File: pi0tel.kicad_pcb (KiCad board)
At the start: 2 copper layers, 10 parts, among them J1 DIN-5_180degree, J2 RPi_GPIO, Q1 BSS138, U1 LM2596S-5

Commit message: grrr
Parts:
- removed 10k1: R, Resistor_SMD:R_0805_2012Metric_Pad1.15x1.40mm_HandSolder
- added ?: , RPi_Hat:RPi_Hat_Mounting_Hole, F.Cu at (16.0, 51.0)
- added ?: , RPi_Hat:RPi_Hat_Mounting_Hole, F.Cu at (74.0, 28.0)
- added ?: , RPi_Hat:RPi_Hat_Mounting_Hole, F.Cu at (74.0, 51.0)
- added ?: , RPi_Hat:RPi_Hat_Mounting_Hole, F.Cu at (16.0, 28.0)
- added R2: 10k, Resistor_SMD:R_0805_2012Metric_Pad1.15x1.40mm_HandSolder, F.Cu at (48.3, 34.3)
- moved Q1 100.5 mm to (54.6, 34.3), turned to 180 degrees
- moved R1 100.5 mm to (62.2, 34.3), turned to 180 degrees
- moved U1 95.2 mm to (27.9, 41.9), turned to 90 degrees
- moved C1 90.6 mm to (17.8, 36.8), turned to 90 degrees
- moved C2 75.4 mm to (20.3, 36.8), turned to 90 degrees
- moved D1 74.4 mm to (15.2, 36.8), turned to 90 degrees
- moved L1 57.3 mm to (41.9, 47.0), turned to 270 degrees
- moved J2 47.7 mm to (20.9, 29.3), turned to 90 degrees
- moved J1 22.8 mm to (59.7, 47.0), turned to 180 degrees
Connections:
- C1 pad 1: GND -> /MinitelVcc
- J1 pad 5: GND -> /MinitelVcc
- U1 pad 1: GND -> /MinitelVcc
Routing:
- net /MinitelRx: track 0.00 -> 46.9 mm
- net +5V: track 0.00 -> 40.7 mm
- net Net-(D1-Pad1): track 0.00 -> 36.3 mm
- net /PiRx: track 0.00 -> 34.6 mm
- net /MinitelTx: track 0.00 -> 12.7 mm
- net /MinitelVcc: track 0.00 -> 12.6 mm
- added copper zone on F.Cu, net +3V3
- added copper zone on B.Cu, net GND
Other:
- board outline added: 65 x 30 mm
- net class Default: via_dia 0.8 -> 0.6
- rule pad_to_mask_clearance: 0.051 -> 0
- rule trace_min: 0.2 -> 0.01

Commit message: hmmm
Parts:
- J1: footprint footprints:din_5_econet_pcb_mount -> myelin-kicad:din_5_econet_pcb_mount
- moved C2 40.8 mm to (61.0, 40.6)
- moved D1 40.7 mm to (55.9, 34.3)
- moved R1 33.0 mm to (29.2, 33.0), turned to 90 degrees
- moved Q1 31.4 mm to (23.2, 34.1)
- moved J1 30.5 mm to (29.2, 47.0)
- moved L1 29.0 mm to (69.8, 39.4), turned to 90 degrees
- moved U1 21.9 mm to (49.5, 45.7), turned to 0 degrees
- moved C1 21.9 mm to (39.4, 33.0), turned to 0 degrees
- moved R2 18.5 mm to (43.2, 52.1), turned to 180 degrees
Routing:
- net +5V: track 40.7 -> 95.1 mm
- net /MinitelRx: track 46.9 -> 22.0 mm
- net /PiRx: track 34.6 -> 11.4 mm
- net /MinitelVcc: track 12.6 -> 32.7 mm
- net /MinitelTx: track 12.7 -> 32.7 mm
- net +3V3: track 0.00 -> 12.6 mm
- net GND: track 0.00 -> 10.9 mm
- net Net-(D1-Pad1): track 36.3 -> 31.9 mm
- added copper zone on F.Cu, net GND
- removed copper zone on F.Cu, net +3V3

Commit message: getting there
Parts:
- C1: value 680uF -> 270uF; footprint Capacitor_SMD:C_1206_3216Metric_Pad1.42x1.75mm_HandSolder -> Capacitor_SMD:CP_Elec_8x10.5
- C2: value 220uF -> 470uF; footprint Capacitor_SMD:C_1206_3216Metric_Pad1.42x1.75mm_HandSolder -> Capacitor_SMD:CP_Elec_8x10.5
- L1: value 33uH -> 68uH; footprint Inductor_SMD:L_12x12mm_H6mm -> Inductor_SMD:L_Bourns_SRR1260
- moved J1 41.7 mm to (70.2, 39.5), turned to 270 degrees
- moved C2 40.7 mm to (20.3, 38.1), turned to 0 degrees
- moved Q1 35.1 mm to (57.7, 40.6), turned to 270 degrees
- moved R1 28.5 mm to (57.7, 34.3), turned to 180 degrees
- moved L1 25.2 mm to (46.2, 48.3), turned to 0 degrees
- moved U1 18.1 mm to (31.5, 44.2), turned to 270 degrees
- moved D1 16.7 mm to (39.6, 38.1)
- moved R2 15.4 mm to (57.7, 47.0), turned to 0 degrees
- moved C1 10.5 mm to (48.8, 37.6), turned to 180 degrees
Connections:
- J2 pad 1: +3V3 -> Net-(J2-Pad1)
- J2 pad 17: Net-(J2-Pad17) -> +3V3
- J2 pad 25: GND -> Net-(J2-Pad25)
- J2 pad 4: Net-(J2-Pad4) -> +5V
- J2 pad 9: Net-(J2-Pad9) -> GND
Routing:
- net +5V: track 95.1 -> 65.4 mm
- net GND: track 10.9 -> 38.7 mm, vias 0 -> 40
- net /PiRx: track 11.4 -> 34.7 mm
- net /MinitelTx: track 32.7 -> 12.6 mm
- net /MinitelRx: track 22.0 -> 42.1 mm
- net +3V3: track 12.6 -> 25.0 mm
- net Net-(D1-Pad1): track 31.9 -> 25.7 mm
- net /MinitelVcc: track 32.7 -> 37.2 mm, vias 0 -> 1
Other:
- net class Largish added: clearance 0.2, trace_width 0.4, via_dia 0.6, via_drill 0.4

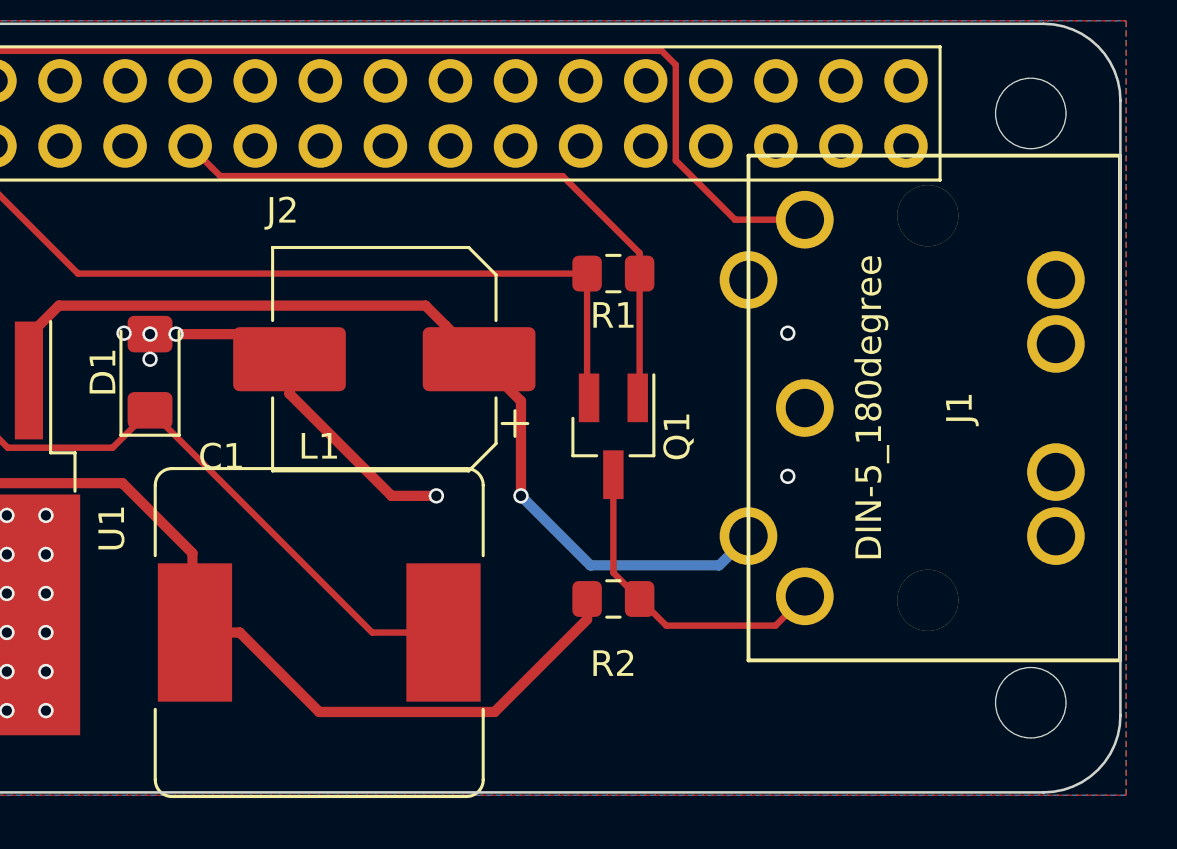
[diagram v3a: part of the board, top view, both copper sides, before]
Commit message: Move din to the back
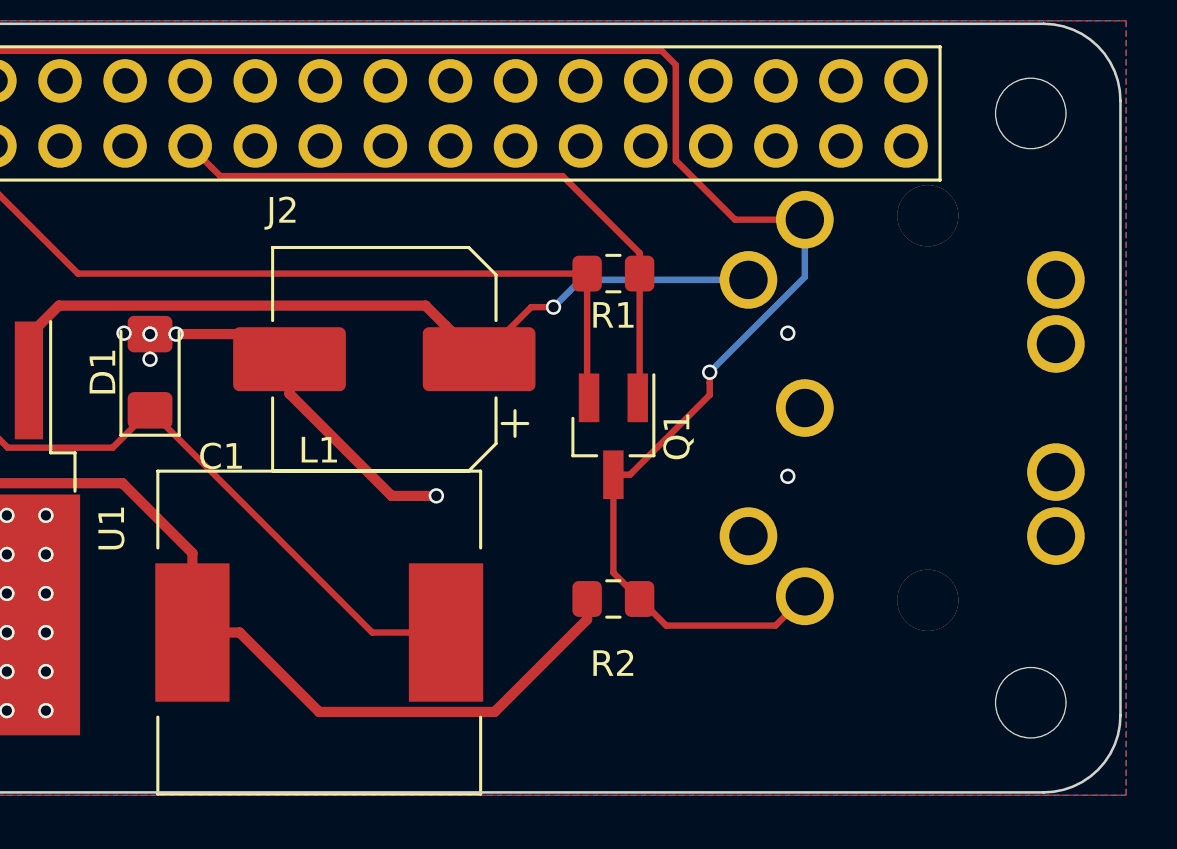
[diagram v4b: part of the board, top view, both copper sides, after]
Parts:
- J1: moved to B.Cu
- L1: footprint Inductor_SMD:L_Bourns_SRR1260 -> Inductor_SMD:L_12x12mm_H6mm
- turned J1 to 90 degrees
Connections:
- J2 pad 20: Net-(J2-Pad20) -> GND
- J2 pad 25: Net-(J2-Pad25) -> GND
- J2 pad 30: Net-(J2-Pad30) -> GND
- J2 pad 34: Net-(J2-Pad34) -> GND
- J2 pad 39: Net-(J2-Pad39) -> GND
- J2 pad 4: +5V -> Net-(J2-Pad4)
- J2 pad 6: Net-(J2-Pad6) -> GND
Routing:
- net /MinitelTx: track 12.6 -> 26.1 mm, vias 0 -> 1
- net /MinitelVcc: track 37.2 -> 32.5 mm

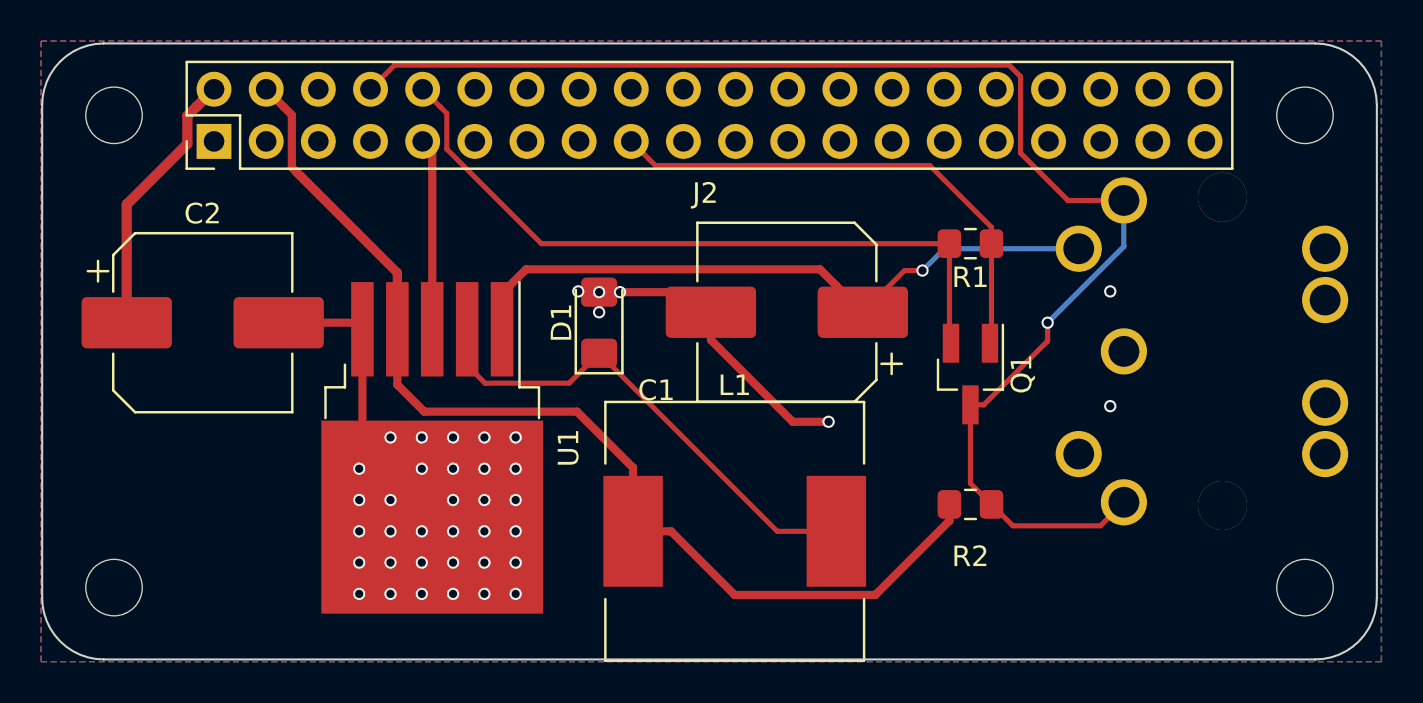
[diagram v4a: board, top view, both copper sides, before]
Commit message: Move footprints around to match more closely how usual layouts look.
See for instance
https://img.gkbcdn.com/s3/p/2015-05-22/lm2596-5v-buck-converter-7-30v-to-5v-step-down-regulator-module-for-diy-project-1571986804286.jpg
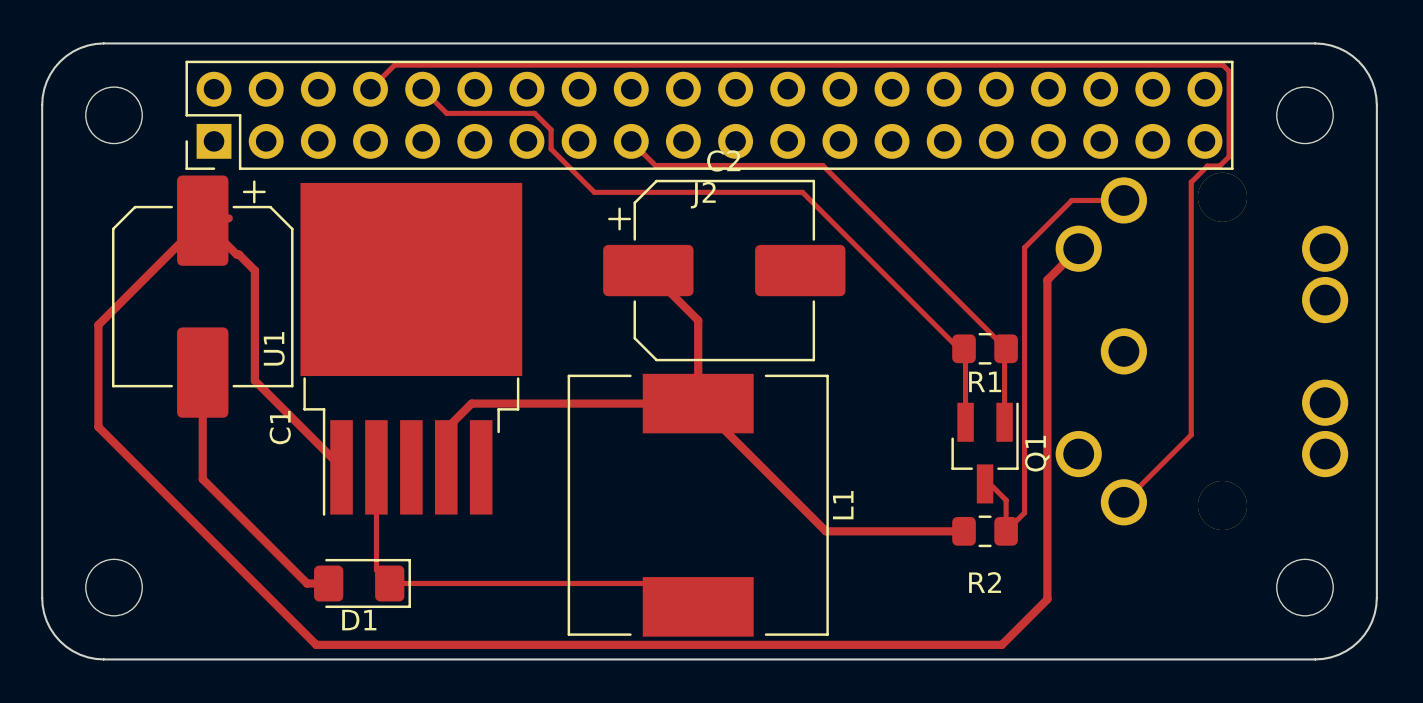
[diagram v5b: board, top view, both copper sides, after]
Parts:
- moved C1 28.5 mm to (20.3, 36.8), turned to 270 degrees
- moved C2 25.5 mm to (45.7, 35.6)
- moved D1 17.3 mm to (27.9, 50.8), turned to 180 degrees
- moved R1 5.17 mm to (58.4, 39.4)
- moved U1 4.93 mm to (30.5, 39.4), turned to 90 degrees
- moved Q1 3.92 mm to (58.4, 44.5)
- moved L1 2.18 mm to (44.5, 47.0), turned to 270 degrees
- moved R2 1.49 mm to (58.4, 48.3)
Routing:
- net /MinitelVcc: track 32.5 -> 97.9 mm, vias 1 -> 0
- net +5V: track 65.4 -> 37.7 mm
- net GND: track 38.7 -> 13.4 mm, vias 40 -> 0
- net /MinitelRx: track 42.1 -> 65.9 mm
- net Net-(D1-Pad1): track 25.7 -> 21.4 mm
- net /MinitelTx: track 26.1 -> 22.8 mm, vias 1 -> 0
- net +3V3: track 25.0 -> 26.0 mm
- net /PiRx: track 34.7 -> 35.8 mm
- removed copper zone on B.Cu, net GND
- removed copper zone on F.Cu, net GND

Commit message: Ground plane
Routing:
- net +5V: track 37.7 -> 63.1 mm
- net GND: vias 0 -> 46
- added copper zone on B.Cu, net GND
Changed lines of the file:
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@@
     (thickness 1.6)
     (drawings 16)
-    (tracks 60)
+    (tracks 113)
     (zones 0)
     (modules 14)
@@
   (gr_line (start 15.5 54.5) (end 74.5 54.5) (angle 90) (layer Edge.Cuts) (width 0.1))
   (gr_line (start 77.5 27.5) (end 77.5 51.5) (angle 90) (layer Edge.Cuts) (width 0.1))
+  (via (at 33.8455 45.72) (size 0.6) (drill 0.4) (layers F.Cu B.Cu) (net 4))
+  (via (at 30.48 45.72) (size 0.6) (drill 0.4) (layers F.Cu B.Cu) (net 4))
+  (via (at 34.29 39.37) (size 0.6) (drill 0.4) (layers F.Cu B.Cu) (net 4))
+  (via (at 33.02 39.37) (size 0.6) (drill 0.4) (layers F.Cu B.Cu) (net 4))
+  (via (at 31.75 39.37) (size 0.6) (drill 0.4) (layers F.Cu B.Cu) (net 4))
+  (via (at 30.48 39.37) (size 0.6) (drill 0.4) (layers F.Cu B.Cu) (net 4))
+  (via (at 29.21 39.37) (size 0.6) (drill 0.4) (layers F.Cu B.Cu) (net 4))
+  (via (at 27.94 39.37) (size 0.6) (drill 0.4) (layers F.Cu B.Cu) (net 4))
+  (via (at 26.67 39.37) (size 0.6) (drill 0.4) (layers F.Cu B.Cu) (net 4))
+  (via (at 26.67 33.02) (size 0.6) (drill 0.4) (layers F.Cu B.Cu) (net 4))
+  (via (at 27.94 33.02) (size 0.6) (drill 0.4) (layers F.Cu B.Cu) (net 4))
+  (via (at 29.21 33.02) (size 0.6) (drill 0.4) (layers F.Cu B.Cu) (net 4))
+  (via (at 30.48 33.02) (size 0.6) (drill 0.4) (layers F.Cu B.Cu) (net 4))
+  (via (at 31.75 33.02) (size 0.6) (drill 0.4) (layers F.Cu B.Cu) (net 4))
+  (via (at 33.02 33.02) (size 0.6) (drill 0.4) (layers F.Cu B.Cu) (net 4))
+  (via (at 34.29 33.02) (size 0.6) (drill 0.4) (layers F.Cu B.Cu) (net 4))
+  (via (at 34.29 34.29) (size 0.6) (drill 0.4) (layers F.Cu B.Cu) (net 4))
+  (via (at 33.02 34.29) (size 0.6) (drill 0.4) (layers F.Cu B.Cu) (net 4))
+  (via (at 31.75 34.29) (size 0.6) (drill 0.4) (layers F.Cu B.Cu) (net 4))
+  (via (at 30.48 34.29) (size 0.6) (drill 0.4) (layers F.Cu B.Cu) (net 4))
+  (via (at 29.21 34.29) (size 0.6) (drill 0.4) (layers F.Cu B.Cu) (net 4))
+  (via (at 27.94 34.29) (size 0.6) (drill 0.4) (layers F.Cu B.Cu) (net 4))
+  (via (at 26.67 34.29) (size 0.6) (drill 0.4) (layers F.Cu B.Cu) (net 4))
+  (via (at 26.67 38.1) (size 0.6) (drill 0.4) (layers F.Cu B.Cu) (net 4))
+  (via (at 27.94 38.1) (size 0.6) (drill 0.4) (layers F.Cu B.Cu) (net 4))
+  (via (at 29.21 38.1) (size 0.6) (drill 0.4) (layers F.Cu B.Cu) (net 4))
+  (via (at 30.48 38.1) (size 0.6) (drill 0.4) (layers F.Cu B.Cu) (net 4))
+  (via (at 31.75 38.1) (size 0.6) (drill 0.4) (layers F.Cu B.Cu) (net 4))
+  (via (at 33.02 38.1) (size 0.6) (drill 0.4) (layers F.Cu B.Cu) (net 4))
+  (via (at 34.29 38.1) (size 0.6) (drill 0.4) (layers F.Cu B.Cu) (net 4))
+  (via (at 34.29 36.83) (size 0.6) (drill 0.4) (layers F.Cu B.Cu) (net 4))
+  (via (at 33.02 36.83) (size 0.6) (drill 0.4) (layers F.Cu B.Cu) (net 4))
+  (via (at 31.75 36.83) (size 0.6) (drill 0.4) (layers F.Cu B.Cu) (net 4))
+  (via (at 30.48 36.83) (size 0.6) (drill 0.4) (layers F.Cu B.Cu) (net 4))
+  (via (at 29.21 36.83) (size 0.6) (drill 0.4) (layers F.Cu B.Cu) (net 4))
+  (via (at 27.94 36.83) (size 0.6) (drill 0.4) (layers F.Cu B.Cu) (net 4))
+  (via (at 26.67 36.83) (size 0.6) (drill 0.4) (layers F.Cu B.Cu) (net 4))
+  (via (at 26.67 35.56) (size 0.6) (drill 0.4) (layers F.Cu B.Cu) (net 4))
+  (via (at 27.94 35.56) (size 0.6) (drill 0.4) (layers F.Cu B.Cu) (net 4))
+  (via (at 34.29 35.56) (size 0.6) (drill 0.4) (layers F.Cu B.Cu) (net 4))
+  (via (at 33.02 35.56) (size 0.6) (drill 0.4) (layers F.Cu B.Cu) (net 4))
+  (via (at 31.75 35.56) (size 0.6) (drill 0.4) (layers F.Cu B.Cu) (net 4))
+  (via (at 29.21 35.56) (size 0.6) (drill 0.4) (layers F.Cu B.Cu) (net 4))
+  (via (at 30.48 35.56) (size 0.6) (drill 0.4) (layers F.Cu B.Cu) (net 4))
+  (via (at 26.67 50.8) (size 0.6) (drill 0.4) (layers F.Cu B.Cu) (net 4))
+  (via (at 50.8 35.56) (size 0.6) (drill 0.4) (layers F.Cu B.Cu) (net 4))
   (segment (start 33.414998 42.04) (end 44.45 42.04) (width 0.4) (layer F.Cu) (net 2))
   (segment (start 32.18 43.274998) (end 33.414998 42.04) (width 0.4) (layer F.Cu) (net 2))
@@
   (segment (start 50.67 48.26) (end 44.45 42.04) (width 0.4) (layer F.Cu) (net 2))
   (segment (start 57.395 48.26) (end 50.67 48.26) (width 0.4) (layer F.Cu) (net 2))
+  (segment (start 22.159999 28.019999) (end 20.87 26.73) (width 0.4) (layer F.Cu) (net 2))
+  (segment (start 29.090001 28.019999) (end 22.159999 28.019999) (width 0.4) (layer F.Cu) (net 2))
+  (segment (start 29.779999 28.709997) (end 29.090001 28.019999) (width 0.4) (layer F.Cu) (net 2))
+  (segment (start 29.779999 29.870001) (end 29.779999 28.709997) (width 0.4) (layer F.Cu) (net 2))
+  (segment (start 30.804997 30.894999) (end 29.779999 29.870001) (width 0.4) (layer F.Cu) (net 2))
+  (segment (start 37.354999 30.894999) (end 30.804997 30.894999) (width 0.4) (layer F.Cu) (net 2))
+  (segment (start 42.02 35.56) (end 37.354999 30.894999) (width 0.4) (layer F.Cu) (net 2))
   (segment (start 59.445 48.26) (end 59.445 46.745) (width 0.25) (layer F.Cu) (net 3))
   (segment (start 58.65 45.95) (end 58.42 45.95) (width 0.25) (layer F.Cu) (net 3))
@@
   (segment (start 61.455999 36.022001) (end 62.981 34.497) (width 0.4) (layer F.Cu) (net 36))
   (segment (start 59.239999 53.790001) (end 61.455999 51.574001) (width 0.4) (layer F.Cu) (net 36))
+  (zone (net 4) (net_name GND) (layer B.Cu) (hatch edge 0.508)
+    (connect_pads (clearance 0.508))
+    (min_thickness 0.254)
+    (fill yes (arc_segments 32) (thermal_gap 0.508) (thermal_bridge_width 0.508))
+    (polygon
+      (pts
+        (xy 77.47 54.61) (xy 12.7 54.61) (xy 12.7 24.13) (xy 77.47 24.13)
+      )
+    )
+  )
 )
